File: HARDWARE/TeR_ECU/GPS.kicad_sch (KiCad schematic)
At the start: 16 parts, among them J5 GPS_ANT, U10 NEO-M9N

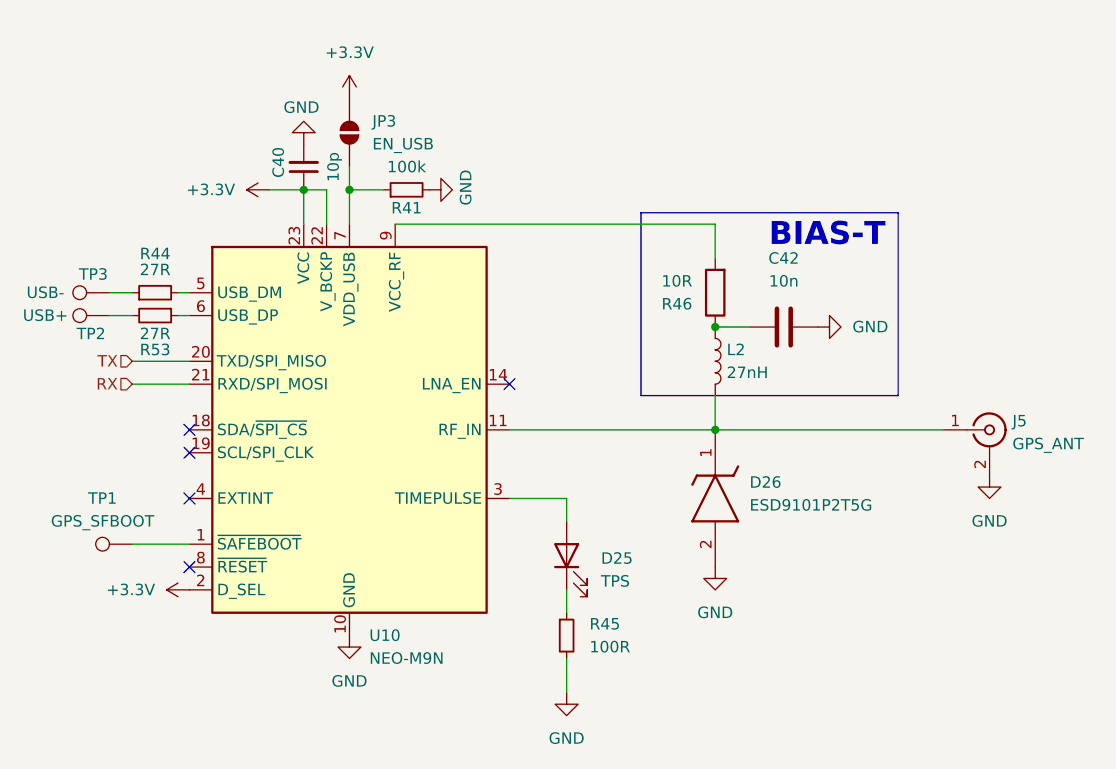
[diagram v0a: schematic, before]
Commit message: Corregidos conectores, CAN y añadidas librerias al proyecto para cargar huellas
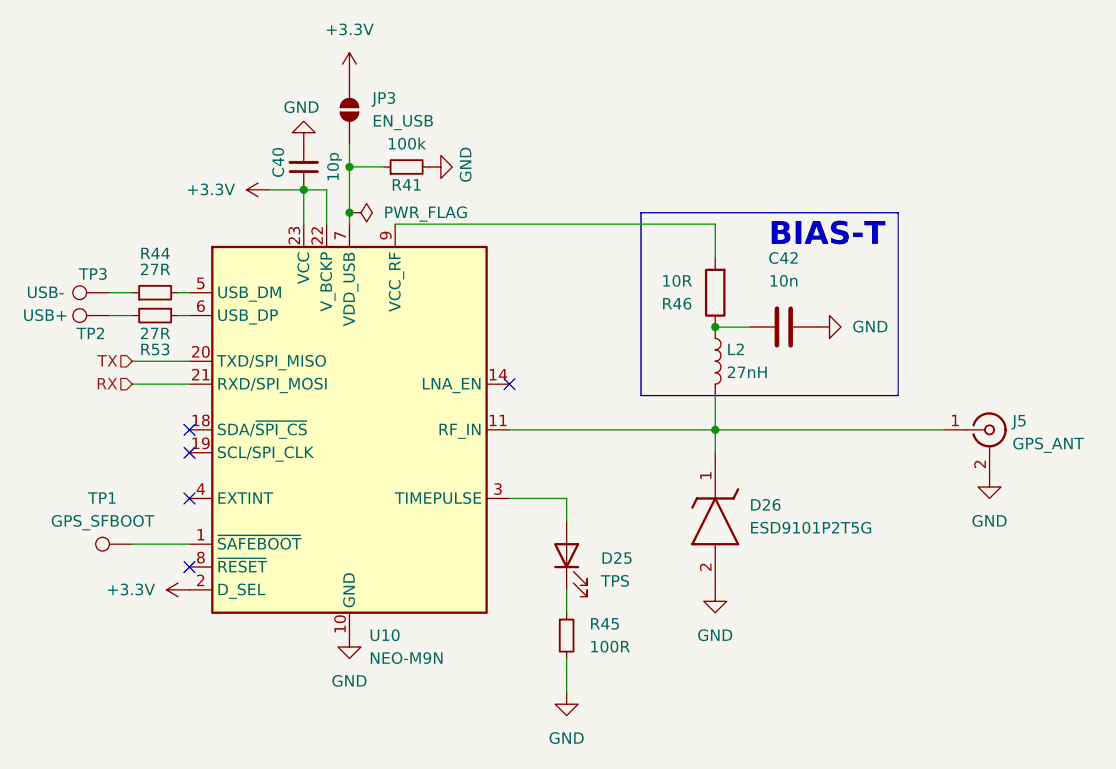
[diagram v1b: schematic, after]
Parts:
- D26: footprint GPS_D:SODFL1006X40N -> ESD9101:SODFL1006X40N
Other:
- moved on the sheet: D26, JP3, R41
